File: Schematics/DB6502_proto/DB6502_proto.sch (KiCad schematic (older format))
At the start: 23 parts, among them U1 71256, U2 71256, U3 28C256, U4 65C02S, U5 74AC74, U6 74AC138, U7 22V10C, U8 74AC04, U9 74HC21

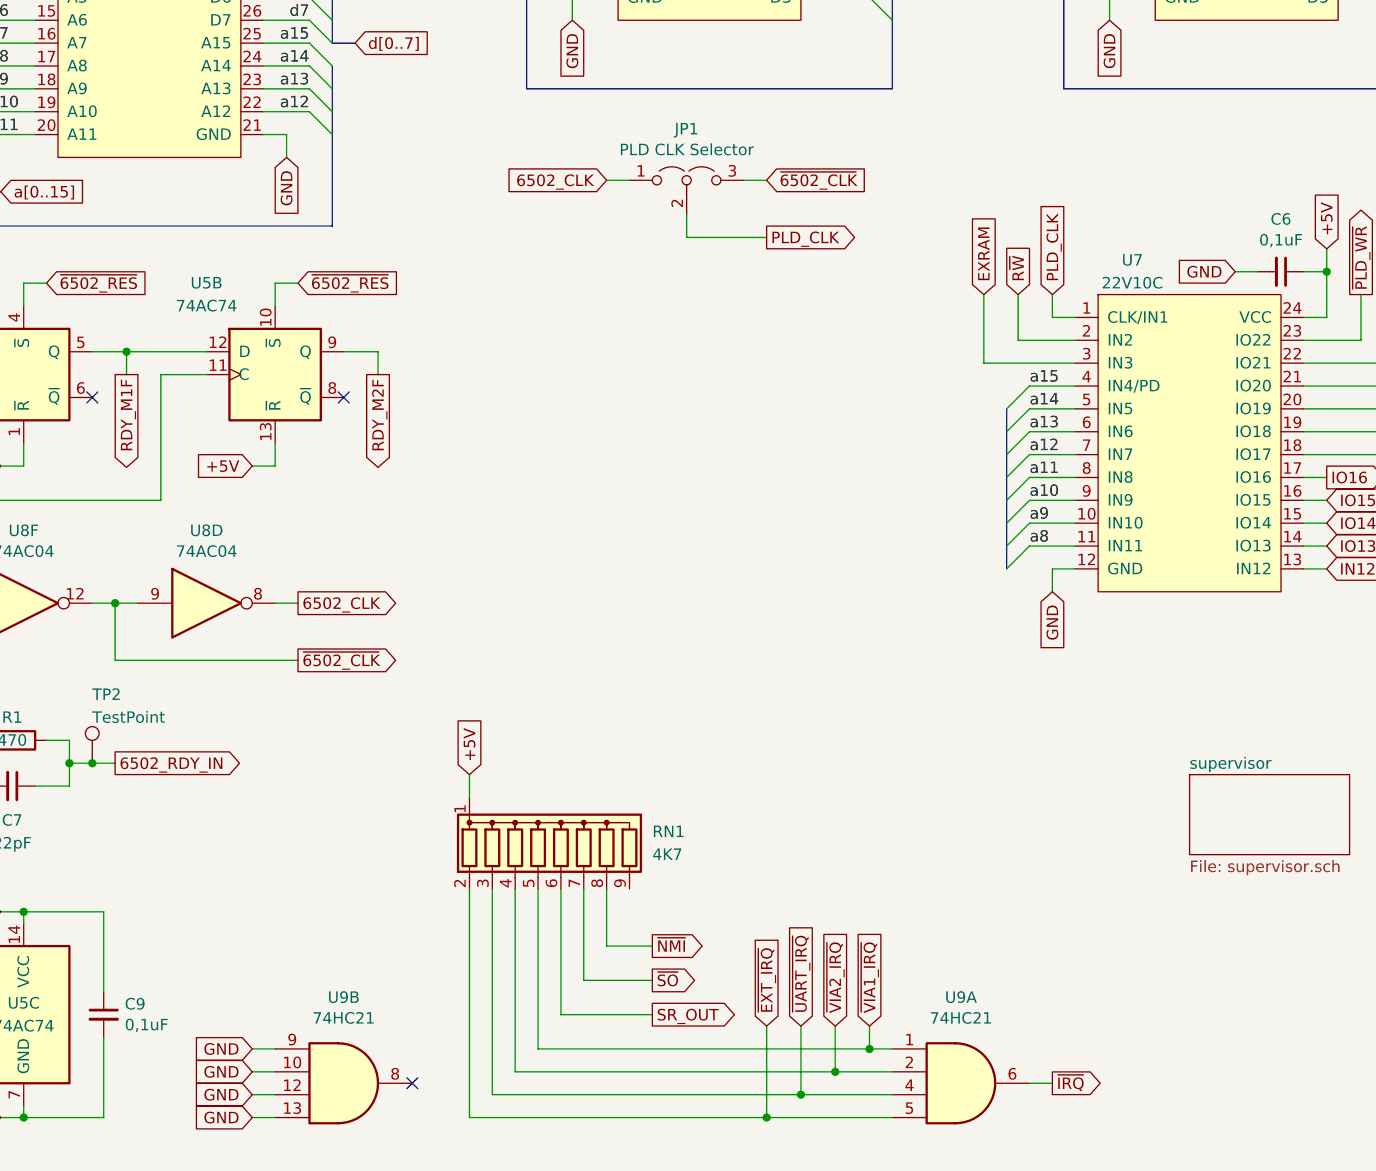
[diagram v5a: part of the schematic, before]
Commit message: Added latch feature for EXRAM
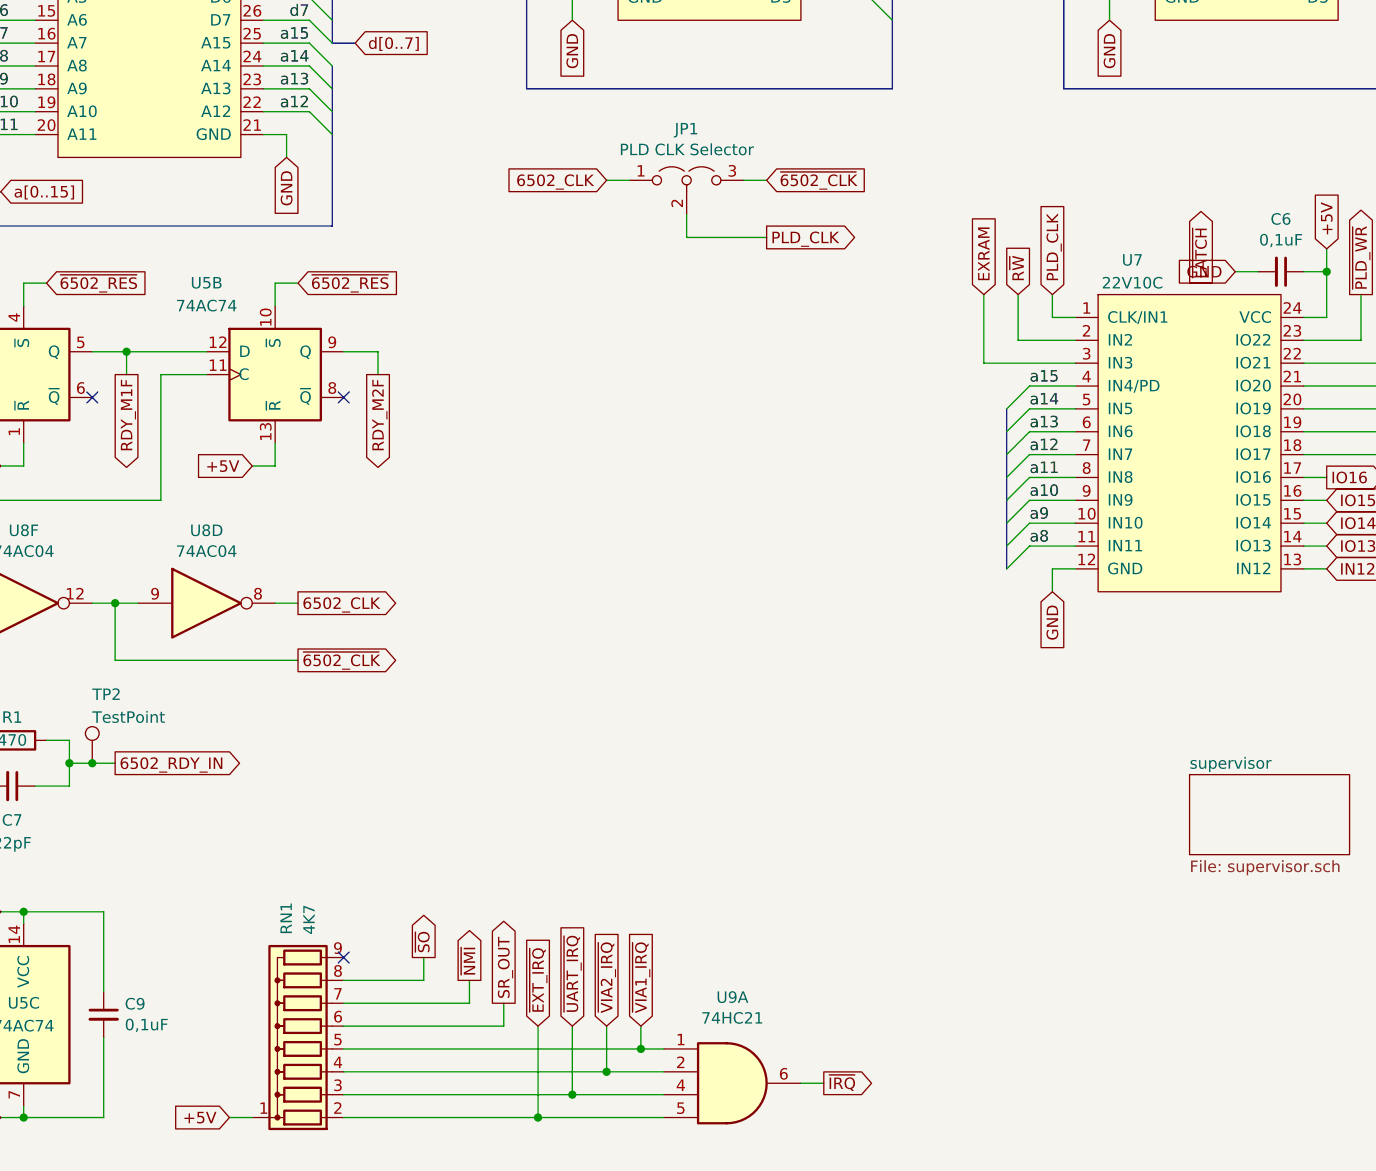
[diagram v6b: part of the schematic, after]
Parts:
- removed unit 2 of U9
- R1: footprint Resistor_THT:R_Axial_DIN0207_L6.3mm_D2.5mm_P10.16mm_Horizontal -> Resistor_SMD:R_1206_3216Metric_Pad1.42x1.75mm_HandSolder
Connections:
- net ~NMI: now also RN1.7 (R6); no longer RN1.8 (R7)
- net ~SO: now also RN1.8 (R7); no longer RN1.7 (R6)
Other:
- moved on the sheet: RN1, U9A
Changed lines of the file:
@@
 L 74xx:74LS21 U9
 U 1 1 5FB20233
-P 5950 7300
-F 0 "U9" H 5950 7675 50  0000 C CNN
-F 1 "74HC21" H 5950 7584 50  0000 C CNN
-F 2 "Package_SO:SOIC-14_3.9x8.7mm_P1.27mm" H 5950 7300 50  0001 C CNN
-F 3 "http://www.ti.com/lit/gpn/sn74LS21" H 5950 7300 50  0001 C CNN
-	1    5950 7300
-	1    0    0    -1
-$EndComp
-$Comp
-L 74xx:74LS21 U9
-U 2 1 5FB22533
-P 3250 7300
-F 0 "U9" H 3250 7675 50  0000 C CNN
-F 1 "74HC21" H 3250 7584 50  0000 C CNN
-F 2 "Package_SO:SOIC-14_3.9x8.7mm_P1.27mm" H 3250 7300 50  0001 C CNN
-F 3 "http://www.ti.com/lit/gpn/sn74LS21" H 3250 7300 50  0001 C CNN
-	2    3250 7300
+P 4950 7300
+F 0 "U9" H 4950 7675 50  0000 C CNN
+F 1 "74HC21" H 4950 7584 50  0000 C CNN
+F 2 "Package_SO:SOIC-14_3.9x8.7mm_P1.27mm" H 4950 7300 50  0001 C CNN
+F 3 "http://www.ti.com/lit/gpn/sn74LS21" H 4950 7300 50  0001 C CNN
+	1    4950 7300
 	1    0    0    -1
 $EndComp
@@
 Wire Wire Line
 	1000 7550 1000 7500
-Text GLabel 5550 7050 1    50   Input ~ 0
+Text GLabel 4550 7050 1    50   Input ~ 0
 ~VIA1_IRQ
 Wire Wire Line
-	5550 7050 5550 7150
-Wire Wire Line
-	5550 7150 5650 7150
-Text GLabel 5250 7050 1    50   Input ~ 0
+	4550 7050 4550 7150
+Wire Wire Line
+	4550 7150 4650 7150
+Text GLabel 4250 7050 1    50   Input ~ 0
 ~UART_IRQ
-Text GLabel 5100 7050 1    50   Input ~ 0
+Text GLabel 4100 7050 1    50   Input ~ 0
 ~EXT_IRQ
-Text GLabel 6350 7300 2    50   Output ~ 0
+Text GLabel 5350 7300 2    50   Output ~ 0
 ~IRQ
 Wire Wire Line
-	6250 7300 6350 7300
-Wire Wire Line
-	5400 7250 5650 7250
-Wire Wire Line
-	5250 7050 5250 7350
-Wire Wire Line
-	5250 7350 5650 7350
-Wire Wire Line
-	5100 7050 5100 7450
-Wire Wire Line
-	5100 7450 5650 7450
-Text GLabel 3800 5950 1    50   Input ~ 0
+	5250 7300 5350 7300
+Wire Wire Line
+	4400 7250 4650 7250
+Wire Wire Line
+	4250 7050 4250 7350
+Wire Wire Line
+	4250 7350 4650 7350
+Wire Wire Line
+	4100 7050 4100 7450
+Wire Wire Line
+	4100 7450 4650 7450
+Text GLabel 2750 7450 0    50   Input ~ 0
 +5V
-Text GLabel 2850 7150 0    50   Input ~ 0
-GND
-Text GLabel 2850 7250 0    50   Input ~ 0
-GND
-Text GLabel 2850 7350 0    50   Input ~ 0
-GND
-Text GLabel 2850 7450 0    50   Input ~ 0
-GND
-Wire Wire Line
-	2850 7450 2950 7450
-Wire Wire Line
-	2850 7350 2950 7350
-Wire Wire Line
-	2850 7250 2950 7250
-Wire Wire Line
-	2850 7150 2950 7150
-NoConn ~ 3550 7300
 $Comp
 L 74xx:74HC74 U?
@@
 Wire Wire Line
 	10200 1000 10200 1250
-Text GLabel 5400 7050 1    50   Input ~ 0
+Text GLabel 4400 7050 1    50   Input ~ 0
 ~VIA2_IRQ
 Wire Wire Line
-	5400 7050 5400 7250
+	4400 7050 4400 7250
 Wire Wire Line
 	3400 4100 3250 4100
@@
 F 0 "R1" V 1700 5800 50  0000 C CNN
 F 1 "470" V 1800 5800 50  0000 C CNN
-F 2 "Resistor_THT:R_Axial_DIN0207_L6.3mm_D2.5mm_P10.16mm_Horizontal" V 1730 5800 50  0001 C CNN
+F 2 "Resistor_SMD:R_1206_3216Metric_Pad1.42x1.75mm_HandSolder" V 1730 5800 50  0001 C CNN
 F 3 "~" H 1800 5800 50  0001 C CNN
 	1    1800 5800
@@
 L Device:R_Network08 RN1
 U 1 1 6054D542
-P 4200 6250
-F 0 "RN1" H 4600 6300 50  0000 L CNN
-F 1 "4K7" H 4600 6200 50  0000 L CNN
-F 2 "Resistor_THT:R_Array_SIP9" V 4475 6250 50  0001 C CNN
-F 3 "http://www.vishay.com/docs/31509/csc.pdf" H 4200 6250 50  0001 C CNN
-	1    4200 6250
-	1    0    0    -1
-$EndComp
-Wire Wire Line
-	3800 5950 3800 6050
-Wire Wire Line
-	4100 6450 4100 7150
-Wire Wire Line
-	4100 7150 5550 7150
-Connection ~ 5550 7150
-Wire Wire Line
-	4000 6450 4000 7250
-Wire Wire Line
-	4000 7250 5400 7250
-Connection ~ 5400 7250
-Wire Wire Line
-	3900 6450 3900 7350
-Wire Wire Line
-	3900 7350 5250 7350
-Connection ~ 5250 7350
-Wire Wire Line
-	3800 6450 3800 7450
-Wire Wire Line
-	3800 7450 5100 7450
-Connection ~ 5100 7450
-Text GLabel 4600 6700 2    50   Output ~ 0
+P 3050 7050
+F 0 "RN1" H 3450 7100 50  0000 L CNN
+F 1 "4K7" H 3450 7000 50  0000 L CNN
+F 2 "Resistor_THT:R_Array_SIP9" V 3325 7050 50  0001 C CNN
+F 3 "http://www.vishay.com/docs/31509/csc.pdf" H 3050 7050 50  0001 C CNN
+	1    3050 7050
+	0    -1   -1   0
+$EndComp
+Wire Wire Line
+	2750 7450 2850 7450
+Connection ~ 4550 7150
+Connection ~ 4400 7250
+Connection ~ 4250 7350
+Connection ~ 4100 7450
+Text GLabel 3800 6850 1    50   Output ~ 0
 ~NMI
-Wire Wire Line
-	4600 6700 4400 6700
-Wire Wire Line
-	4400 6700 4400 6450
-Text GLabel 4600 6850 2    50   Output ~ 0
+Text GLabel 3600 6750 1    50   Output ~ 0
 ~SO
-Wire Wire Line
-	4300 6450 4300 6850
-Wire Wire Line
-	4300 6850 4600 6850
-Text GLabel 4600 7000 2    50   Output ~ 0
+Text GLabel 3950 6950 1    50   Output ~ 0
 SR_OUT
 Wire Wire Line
-	4600 7000 4200 7000
-Wire Wire Line
-	4200 7000 4200 6450
+	3250 7450 4100 7450
+Wire Wire Line
+	3250 7350 4250 7350
+Wire Wire Line
+	3250 7250 4400 7250
+Wire Wire Line
+	3250 7150 4550 7150
+Wire Wire Line
+	3250 6950 3800 6950
+Wire Wire Line
+	3800 6950 3800 6850
+Wire Wire Line
+	3600 6750 3600 6850
+Wire Wire Line
+	3600 6850 3250 6850
+Wire Wire Line
+	3950 7050 3950 6950
+Wire Wire Line
+	3250 7050 3950 7050
+NoConn ~ 3250 6750
 Wire Bus Line
 	8500 4150 8500 4350
@@
 Wire Bus Line
 	1600 2150 1600 3400
+Text GLabel 7000 3800 1    50   Output ~ 0
+~LATCH
 $EndSCHEMATC

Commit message: Added one last line to the system
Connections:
- net EXT_BE: now reaches RN1.9 (R8)
- no-connect marks 5 -> 4
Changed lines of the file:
@@
 Wire Wire Line
 	3250 7050 3950 7050
-NoConn ~ 3250 6750
-Text GLabel 7000 3800 1    50   Output ~ 0
-~LATCH
+Text GLabel 3450 6650 1    50   Output ~ 0
+EXT_BE
+Wire Wire Line
+	3250 6750 3450 6750
+Wire Wire Line
+	3450 6750 3450 6650
 Wire Bus Line
 	8500 4150 8500 4350
